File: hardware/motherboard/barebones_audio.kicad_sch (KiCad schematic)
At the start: 71 parts, among them J22 SJ2-35894B-SMT-TR, SW4 EC05E1220401, U34 ES8316, U35 TS3A227EYFFR, U37 TPA2012D2RTJT, U75 STM32L433VCT6, U76 PCA9306DCTR, Y6 ABS07-32.768KHZ-T

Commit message: pushed many changes and added dedicated bms module
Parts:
- removed R129: 330k, Resistor_SMD:R_0603_1608Metric, symbol Device:R
- removed R130: 10k, Resistor_SMD:R_0603_1608Metric, symbol Device:R
- removed R250, R251, R252: 4.7k, Resistor_SMD:R_0402_1005Metric, symbol Device:R
- removed SW4: EC05E1220401, barebones:SW-SMD_EC05E1220401, symbol EC05E1220401:EC05E1220401
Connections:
- net AGND is gone; now on net GND: U34.17 (CPGND), U34.23 (AGND), U34.33 (EP), U34.5 (DGND)
- net SCL_AUDIO is gone; now on net I2C7_SCL_M0: R132.2, U35.C3 (SCL)
- net SDA_AUDIO is gone; now on net I2C7_SDA_M0: R218.2, U35.B3 (SDA)
- net ES_LOUT: no longer U34.20 (LOUT)
- net ES_ROUT: no longer U34.19 (ROUT)
- net HP_JACK_RING_2: no longer J22.4, U35.D1 (RING2)
- net HP_JACK_SLEEVE: no longer J22.1, U35.D3 (SLEEVE)
- net VCC_1V8_S0: now also R132.1, R216.1, R217.1, R218.1
- net VCC_3V3_S3: no longer R132.1, R216.1, R217.1, R218.1
- net HP_RING_1: now reaches J22.3
- net HP_RING_1: now also U34.19 (ROUT)
- net EN_CHAN_A_0: no longer names the net of U75.23 (PA0)
- net EN_CHAN_B_0: no longer names the net of U75.24 (PA1)
- net HP_DET_TRIGGER renamed HP_DET
- net HP_INT: no longer names the net of U34.12 (GPIO3)
- net HP_JACK_TIP renamed HP_TIP
- net HP_TIP: now also U34.20 (LOUT)
- net I2S0_LRCK_TX renamed I2S0_LRCK
- net I2S0_SCLK_TX renamed I2S0_SCLK
- new net HP_RING_2: J22.4, U35.D1 (RING2)
- new net HP_SLEEVE: J22.1, U35.D3 (SLEEVE)
- no-connect marks 8 -> 11
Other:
- moved on the sheet: C396, C397, C398, C399, C400, C401, C402, C403, C404, C405, C406, C407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

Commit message: arranged the schematics in every sheet
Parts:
- removed C413, C415, C419, C424: 1uF, Capacitor_SMD:C_0603_1608Metric, symbol Device:C
- added C425, C427, C428, C429: 1uF, Capacitor_SMD:C_0603_1608Metric, symbol Device:C
- added C539: 100nF, Capacitor_SMD:C_0603_1608Metric, symbol Device:C
- added J13, J8: SM02B-GHS-TB_LF__SN_, barebones:JST_SM02B-GHS-TB_LF__SN_, symbol SM02B-GHS-TB_LF__SN_:SM02B-GHS-TB_LF__SN_
- added J19: SM06B-SRSS-TB_LF__SN_, SM06B-SRSS-TB_LF__SN_:JST_SM06B-SRSS-TB_LF__SN_, symbol SM06B-SRSS-TB_LF__SN_:SM06B-SRSS-TB_LF__SN_
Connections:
- net GND: now also C425.2, C427.2, C428.2, C429.2, C539.2, J19.6, J19.S1 (SHIELD), J19.S2 (SHIELD)
- net NRST_90: now also J19.4
- net SWCLK_49: now also J19.3
- net SWDIO_72: now also J19.2
- net SWO_89: now also J19.5
- net VCC_3V3_ALW: now also C539.1, J19.1
- net SPK_OUT_L+ renamed SPK_OUT_L_1+
- net SPK_OUT_L_1+: now also C427.1, J8.1
- net SPK_OUT_L- renamed SPK_OUT_L_1-
- net SPK_OUT_L_1-: now also C425.1, J8.2
- net SPK_OUT_R+ renamed SPK_OUT_R_1+
- net SPK_OUT_R_1+: now also C428.1, J13.1
- net SPK_OUT_R- renamed SPK_OUT_R_1-
- net SPK_OUT_R_1-: now also C429.1, J13.2
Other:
- note added: "AUDIO SUBSYSTEM"
- note added: "EMBEDDED CONTROLLER"
- note added: "LEFT SPEAKER"
- note added: "NOTE THIS CHIPS"
- note added: "RIGHT SPEAKER"
- note added: "finish this connection properly"
- note removed: "DIGITAL MEMS MIC"
- moved on the sheet: C396, C397, C398, C399, C400, C401, C402, C403, C404, C405, C406, C407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

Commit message: connected hierarchical labels with net labels in the root sheet
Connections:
- net NRST_14: now also J19.4
- net NRST_90: no longer J19.4, U75.90 (PB4(NJTRST))
- no-connect marks 11 -> 14
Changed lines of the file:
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@@
 	)
 	(no_connect
+		(at 368.3 154.94)
+	)
+	(no_connect
 		(at 368.3 83.82)
 	)
@@
 	)
 	(no_connect
+		(at 368.3 162.56)
+	)
+	(no_connect
+		(at 427.99 81.28)
+	)
+	(no_connect
 		(at 318.77 60.96)
 	)
@@
 	(wire
 		(pts
-			(xy 427.99 81.28) (xy 454.66 81.28)
-		)
-		(stroke
-			(width 0)
-			(type default)
-		)
-	)
-	(wire
-		(pts
 			(xy 342.9 177.8) (xy 344.17 177.8)
 		)
@@
 	(wire
 		(pts
-			(xy 427.99 83.82) (xy 462.28 83.82)
+			(xy 427.99 83.82) (xy 467.36 83.82)
 		)
 		(stroke
@@
 	(wire
 		(pts
-			(xy 541.02 147.32) (xy 544.83 147.32)
+			(xy 541.02 147.32) (xy 553.72 147.32)
 		)
 		(stroke
@@
 		)
 	)
-	(label "NRST_90"
+	(label "NRST_14"
 		(at 509.27 187.96 0)
 		(effects
@@
 		)
 	)
+	(label "NRST_14"
+		(at 553.72 147.32 180)
+		(effects
+			(font
+				(size 1.27 1.27)
+			)
+			(justify right bottom)
+		)
+	)
 	(label "VDD_50"
 		(at 346.71 180.34 0)
@@
 		)
 	)
+	(label "SWO_89"
+		(at 467.36 83.82 180)
+		(effects
+			(font
+				(size 1.27 1.27)
+			)
+			(justify right bottom)
+		)
+	)
 	(label "INL+"
 		(at 59.69 204.47 0)
@@
 		)
 	)
-	(label "NRST_90"
-		(at 454.66 81.28 180)
-		(effects
-			(font
-				(size 1.27 1.27)
-			)
-			(justify right bottom)
-		)
-	)
 	(label "HP_JACK_RING_2"
 		(at 41.91 113.03 0)
@@
 		)
 	)
-	(hierarchical_label "NRST_14"
-		(shape input)
-		(at 544.83 147.32 0)
-		(effects
-			(font
-				(size 1.27 1.27)
-			)
-			(justify left)
-		)
-	)
 	(hierarchical_label "I2C7_SDA_M0"
 		(shape input)
@@
 		(effects
 			(font
-				(size 1.27 1.27)
-			)
-			(justify left)
-		)
-	)
-	(hierarchical_label "SWO_89"
-		(shape input)
-		(at 462.28 83.82 0)
-		(effects
-			(font

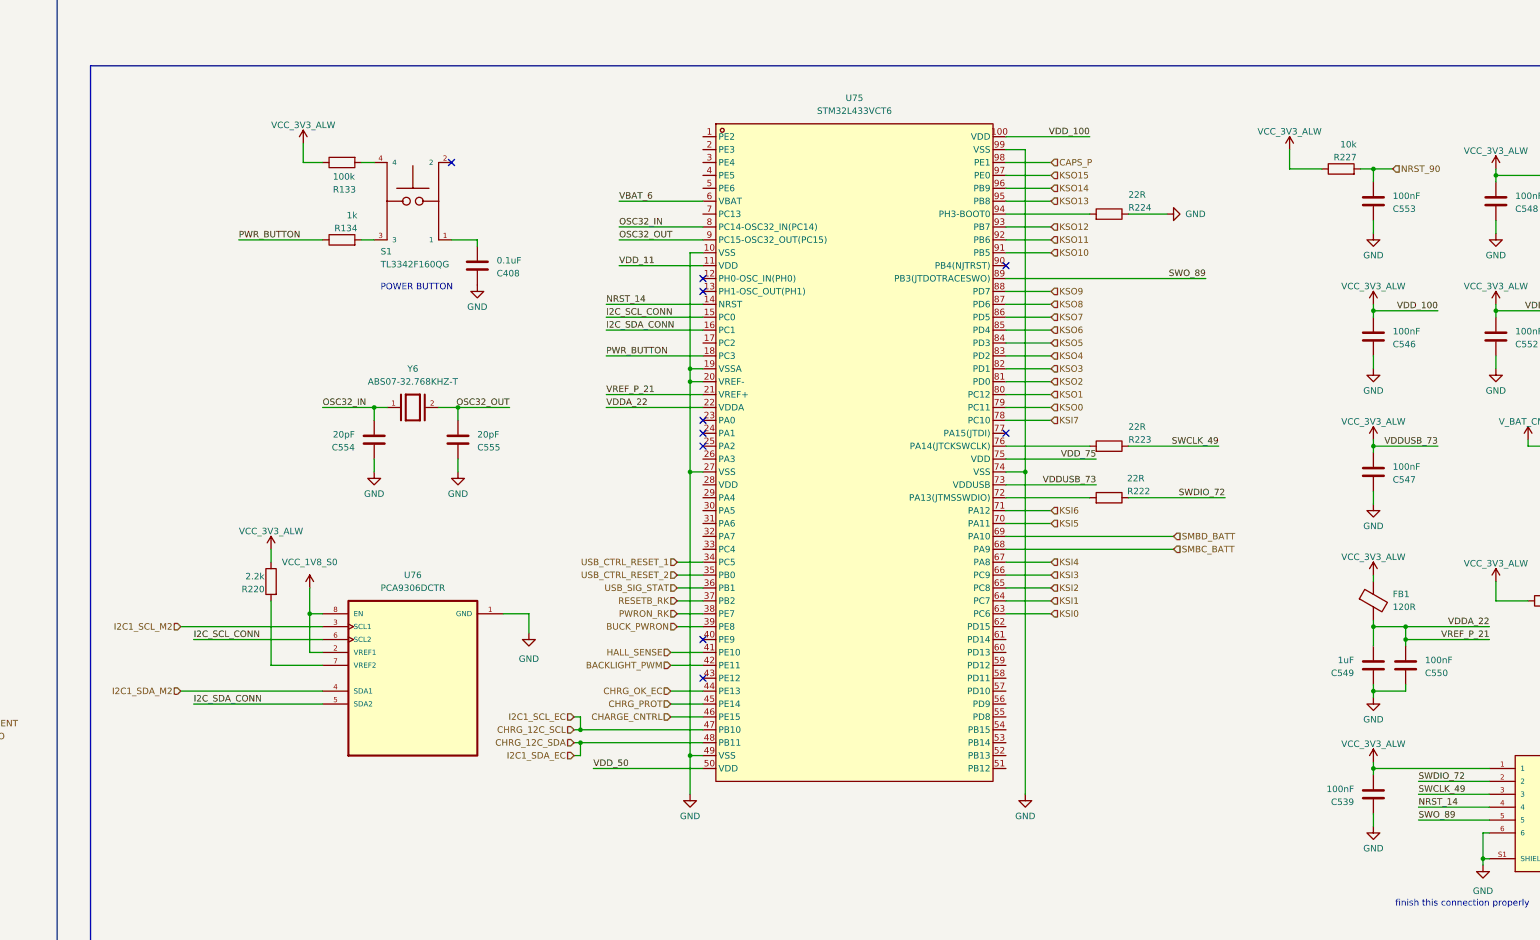
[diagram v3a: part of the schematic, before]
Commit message: removed unused components and connections
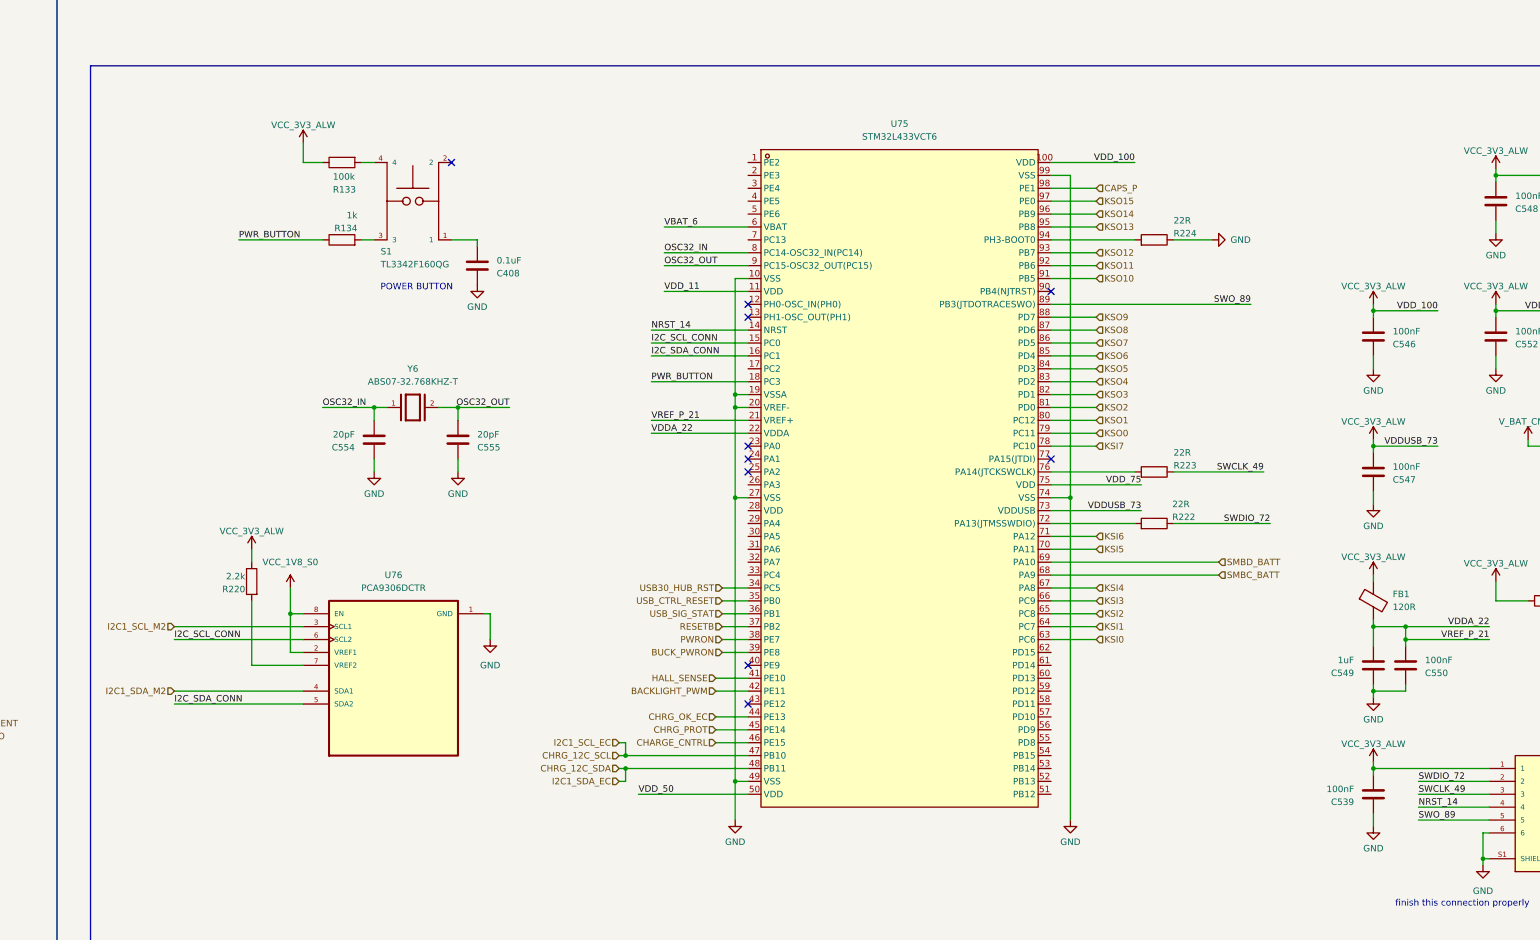
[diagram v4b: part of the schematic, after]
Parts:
- removed C553: 100nF, Capacitor_SMD:C_0603_1608Metric, symbol Device:C
- removed R227: 10k, Resistor_SMD:R_0603_1608Metric, symbol Device:R
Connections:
- net PWRON_RK renamed PWRON
- net RESETB_RK renamed RESETB
- net USB_CTRL_RESET_1 renamed USB30_HUB_RST
- net USB_CTRL_RESET_2 renamed USB_CTRL_RESET
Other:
- moved on the sheet: R220, R222, R223, R224, U75, U76

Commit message: updated last changes
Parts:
- removed C397, C406, C539, C546, C547, C552: 100nF, Capacitor_SMD:C_0603_1608Metric, symbol Device:C
- removed C398: 10uF, Capacitor_SMD:C_0603_1608Metric, symbol Device:C
- removed C414: 1uF, Capacitor_SMD:C_0603_1608Metric, symbol Device:C
- removed C554: 20pF, Capacitor_SMD:C_0603_1608Metric, symbol Device:C
- removed FB1: 120R, Inductor_SMD:L_0402_1005Metric, symbol Device:FerriteBead
- removed J13, J8: SM02B-GHS-TB_LF__SN_, barebones:JST_SM02B-GHS-TB_LF__SN_, symbol SM02B-GHS-TB_LF__SN_:SM02B-GHS-TB_LF__SN_
- removed J22: SJ2-35894B-SMT-TR, barebones:CUI_SJ2-35894B-SMT-TR, symbol SJ2-35894B-SMT-TR:SJ2-35894B-SMT-TR
- removed MK1: SPH0645LM4H-B, barebones:MIC_SPH0645LM4H-B, symbol SPH0645LM4H-B:SPH0645LM4H-B
- removed MK2: CMM-2718AT-3817NC-TR, CMM-2718AT-3817NC-TR:MIC_CMM-2718AT-3817NC-TR, symbol CMM-2718AT-3817NC-TR:CMM-2718AT-3817NC-TR
- removed NT3, NT4: NetTie_2, NetTie:NetTie-2_SMD_Pad0.5mm, symbol Device:NetTie_2
- removed R133: 100k, Resistor_SMD:R_0603_1608Metric, symbol Device:R
- removed R216, R217, R218: 4.7k, Resistor_SMD:R_0603_1608Metric, symbol Device:R
- removed R220: 2.2k, Resistor_SMD:R_0402_1005Metric, symbol Device:R
- removed U75: STM32L433VCT6, barebones:QFP50P1600X1600X160-100N, symbol STM32L433VCT6:STM32L433VCT6
- removed U76: PCA9306DCTR, barebones:SOP65P400X130-8N, symbol PCA9306DCTR:PCA9306DCTR
- added C413, C473, C475, C621, C698, C709, C711, C713, C715, C717, C718, C719, C720, C721, C722: 0.1uF, Capacitor_SMD:C_0201_0603Metric, symbol Device:C
- added C415, C545, C573: 10uF, Capacitor_SMD:C_0603_1608Metric, symbol Device:C
- added C431, C458: 0.1uF, Capacitor_SMD:C_0402_1005Metric, symbol Device:C
- added C477, C478, C574, C615, C707, C708, C710, C712, C714: 1uF, Capacitor_SMD:C_0402_1005Metric, symbol Device:C
- added C544: 4.7uF, Capacitor_SMD:C_0402_1005Metric, symbol Device:C
- added C622: 20pF, Capacitor_SMD:C_0201_0603Metric, symbol Device:C
- added FL2, FL3: BLM18PG121SZ1D, barebones:BEADC1608X95N, symbol BLM18PG121SZ1D:BLM18PG121SZ1D
- added J14, J15: S2B-PH-K-S_LF__SN_, barebones:JST_S2B-PH-K-S_LF__SN_, symbol S2B-PH-K-S_LF__SN_:S2B-PH-K-S_LF__SN_
- added J16: SM04B-SRSS-TB_LF__SN_, barebones:JST_SM04B-SRSS-TB_LF__SN_, symbol SM04B-SRSS-TB_LF__SN_:SM04B-SRSS-TB_LF__SN_
- added J4, J8: SJ3-350114B, barebones:SAMESKY_SJ3-350114B, symbol SJ3-350114B:SJ3-350114B
- added R148, R149: 2.2k, Resistor_SMD:R_0201_0603Metric, symbol Device:R
- added R156, R157, R158: 4.7k, Capacitor_SMD:C_0201_0603Metric, symbol Device:R
- added R192, R193, R243, R244: 10k, Resistor_SMD:R_0201_0603Metric, symbol Device:R
- added U13: STM32U083MCT6, barebones:TQFP-80_L12.0-W12.0-P0.50-LS14.0-BL, symbol STM32U083MCT6:STM32U083MCT6
- added U16, U17: TPS22919DCK, Package_TO_SOT_SMD:SOT-363_SC-70-6, symbol Power_Management:TPS22919DCK
- C396, C408, C555: footprint Capacitor_SMD:C_0603_1608Metric -> Capacitor_SMD:C_0201_0603Metric
- C399, C407, C550, C551, C560: value 100nF -> 0.1uF; footprint Capacitor_SMD:C_0603_1608Metric -> Capacitor_SMD:C_0201_0603Metric
- C403, C412, C418, C420, C423, C426, C428, C429, C542, C549: footprint Capacitor_SMD:C_0603_1608Metric -> Capacitor_SMD:C_0402_1005Metric
- C405, C548: value 100nF -> 10uF
- C425: value 1uF -> 0.1uF; footprint Capacitor_SMD:C_0603_1608Metric -> Capacitor_SMD:C_0201_0603Metric
- C427: value 1uF -> 0.1uF; footprint Capacitor_SMD:C_0603_1608Metric -> Capacitor_SMD:C_0402_1005Metric
- J19: footprint SM06B-SRSS-TB_LF__SN_:JST_SM06B-SRSS-TB_LF__SN_ -> barebones:JST_SM06B-SRSS-TB_LF__SN_
- R131, R134, R141, R219, R221, R222, R223: footprint Resistor_SMD:R_0603_1608Metric -> Resistor_SMD:R_0201_0603Metric
- R132: footprint Resistor_SMD:R_0603_1608Metric -> Capacitor_SMD:C_0201_0603Metric
- R224: value 22R -> 10k; footprint Resistor_SMD:R_0603_1608Metric -> Resistor_SMD:R_0201_0603Metric
- U35: footprint TS3A227EYFFR:BGA16N40P4X4_175X175X62N -> barebones:BGA16N40P4X4_175X175X62N
- Y6: footprint ABS07-32.768KHZ-T:XTAL_ABS07-32.768KHZ-T -> barebones:XTAL_ABS07-32.768KHZ-T
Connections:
- net ES_LOUT is gone; now on net HP_TIP: C418.2
- net ES_ROUT is gone; now on net HP_RING_1: C423.2
- net GNDREF is gone; now on net GND: U34.18 (CPGNDREF)
- net HP_JACK_RING_2 is gone; now on net HP_RING_2: U35.C4 (RING2_SENSE)
- net HP_JACK_SLEEVE is gone; now on net HP_SLEEVE: U35.D4 (SLEEVE_SENSE)
- net VCC_1V8_S0 is gone; now on net AUDIO_PWR_1V8: R132.1, U34.3 (DVDD), U34.4 (PVDD)
- net VCC_ES_CE is gone; now on net AUDIO_PWR_1V8: R219.2
- net BACKLIGHT_PWM: now also U13.30 (PB1)
- net BUCK_PWRON: now also U13.28 (PC5)
- net CAPS_P: now also U13.80 (PB9)
- net CHRG_12C_SCL: now also R244.2, U13.35 (PB10)
- net CHRG_12C_SDA: now also R243.2, U13.36 (PB11)
- net CHRG_OK_EC: now also U13.31 (PB2)
- net CHRG_PROT: now also U13.32 (PE7)
- net DACVREF: now also C415.2; no longer C401.2
- net GND: now also C401.2, C405.2, C425.1, C413.2, C415.1, C431.2, C458.2, C473.2, C475.2, C477.2, C478.2, C544.2, C545.2, C573.2, C621.2, C622.2, C698.2, C707.2, C708.2, C709.2, C710.2, C711.2, C712.2, C713.2, C714.2, C715.2, C717.2, C718.2, C719.2, C720.2, C721.2, C722.2, J16.1, J16.S1 (SHIELD), J16.S2 (SHIELD), J8.1, J8.4_1, J8.4_2, R192.1, R193.1, U13.1 (VSS), U13.14 (VSSA/VREF-), U13.21 (VSS), U13.37 (VSS), U13.59 (VSS), U16.2 (GND), U17.2 (GND); no longer C401.1, C405.1, C425.2, J19.6
- net HALL_SENSE: now also U13.29 (PB0)
- net HP_DET: now also J4.5
- net HP_RING_1: now also J4.3
- net HP_RING_2: now also J4.4_1, J4.4_2
- net HP_SLEEVE: now also J4.1
- net HP_TIP: now also J4.2
- net I2C7_SDA_M0: now also R156.2
- net INT_AUDIO: now also R157.2
- net KSI0: now also U13.46 (PD11)
- net KSI1: now also U13.47 (PD12)
- net KSI2: now also U13.48 (PD13)
- net KSI3: now also U13.49 (PC6)
- net KSI4: now also U13.50 (PC7)
- net KSI5: now also U13.51 (PC8)
- net KSI6: now also U13.52 (PC9)
- net KSI7: now also U13.62 (PA15)
- net KSO0: now also U13.63 (PC10)
- net KSO1: now also U13.64 (PC11)
- net KSO10: now also U13.73 (PB3)
- net KSO11: now also U13.74 (PB4)
- net KSO12: now also U13.75 (PB5)
- net KSO13: now also U13.76 (PB6)
- net KSO14: now also U13.77 (PB7)
- net KSO15: now also U13.79 (PB8)
- net KSO2: now also U13.65 (PC12)
- net KSO3: now also U13.66 (PD0)
- net KSO4: now also U13.67 (PD1)
- net KSO5: now also U13.68 (PD2)
- net KSO6: now also U13.69 (PD3)
- net KSO7: now also U13.70 (PD4)
- net KSO8: now also U13.71 (PD5)
- net KSO9: now also U13.72 (PD6)
- net LIN2: now also C574.1; no longer C405.2
- net MICBIAS: now also R148.1, R149.2
- net MIC_PRESENT: now also R158.2
- net OSC32_IN: now also C622.1, U13.5 (PC14-OSC32_IN)
- net OSC32_OUT: now also U13.6 (PC15-OSC32_OUT)
- net PVDD: now also C431.1, C458.1, C545.1, C573.1, FL2.1
- net PWRON: now also U13.27 (PC4)
- net PWR_BUTTON: now also U13.56 (PA11[PA9])
- net RESETB: now also U13.26 (PA7)
- net RIN2: now also C615.1
- net SMBC_BATT: now also U13.54 (PA9)
- net SMBD_BATT: now also U13.55 (PA10)
- net SPK_OUT_L_1+: now also C477.1, J14.1; no longer C427.1
- net SPK_OUT_L_1-: now also C478.1, J14.2; no longer C425.1
- net SPK_OUT_R_1+: now also J15.1
- net SPK_OUT_R_1-: now also J15.2
- net USB30_HUB_RST: now also U13.23 (PA4)
- net USB_CTRL_RESET: now also U13.24 (PA5)
- net USB_SIG_STAT: now also U13.25 (PA6)
- net VCC_3V3_ALW: now also C621.1, C707.1, C708.1, C709.1, C710.1, C711.1, C712.1, C713.1, C714.1, C715.1, FL3.1, R243.1, R244.1, U13.2 (VDD), U13.22 (VDD), U13.38 (VDD), U13.60 (VDDUSB); no longer C548.1
- net V_BAT_CMOS: now also U13.3 (VBAT)
- net at R223.2: now also U13.61 (PA14)
- net at R222.2: now also U13.58 (PA13)
- net at R224.2: now also U13.78 (PF3-BOOT0)
- net RIN1: now reaches U34.29 (RIN1)
- net RIN1: now also C425.2
- net AVDD renamed AUDIO_PWR_IN
- net AUDIO_PWR_IN: now also C473.1, C544.1, C719.1, U16.5 (QOD), U16.6 (OUT)
- net CPVDD renamed AUDIO_PWR_1V8
- net AUDIO_PWR_1V8: now also C401.1, C405.1, C413.1, C475.1, C722.1, R156.1, R157.1, R158.1, U17.5 (QOD), U17.6 (OUT)
- net NRST_14 renamed NRST
- net NRST: now also U13.9 (PF2-NRST)
- net SWCLK_49 renamed SWCLK
- net SWDIO_72 renamed SWDIO
- net SWO_89 renamed LPUART_TX
- net LPUART_TX: now also U13.19 (PA2)
- net VCC_3V3_S3 renamed VCC_3V3_S0
- net VCC_3V3_S0: now also FL2.2
- net VDDA_22 renamed VDDA
- net VDDA: now also C698.1, FL3.2, U13.15 (VREF+), U13.16 (VDDA)
- new net AUDIO_PWR_1: C720.1, C721.1, R193.2, U17.1 (IN), U17.3 (ON)
- new net AUDIO_PWR_2: C717.1, C718.1, R192.2, U16.1 (IN), U16.3 (ON)
- new net BATT_PRES: U13.34 (PE9)
- new net BK_0_PG: U13.44 (PD9)
- new net BK_1_PG: U13.43 (PD8)
- new net CHRG_CTRL: U13.33 (PE8)
- new net FAN_PWM: J16.2, U13.53 (PA8)
- new net FAN_TACH: J16.4, U13.17 (PA0)
- new net HLL_SENSOR: U13.40 (PB13)
- new net INT_ALS: U13.18 (PA1)
- new net LPUART_RX: J19.6, U13.20 (PA3)
- new net LP_INDICATOR: U13.39 (PB12)
- new net MIC_RING_1: C615.2, J8.3, R148.2
- new net MIC_TIP: C574.2, J8.2, R149.1
- new net VCC_5V0_SYS: C427.1, C548.1, J16.3
- no-connect marks 14 -> 17
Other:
- note removed: "NOTE THIS CHIPS"
- moved on the sheet: C396, C399, C400, C402, C403, C407, C408, C412, C418, C523, C525, C542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

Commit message: started routing on LPDDR4x RAM
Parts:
- removed J14: S2B-PH-K-S_LF__SN_, barebones:JST_S2B-PH-K-S_LF__SN_, symbol S2B-PH-K-S_LF__SN_:S2B-PH-K-S_LF__SN_
- added J5: SM04B-SRSS-TB_LF__SN_, barebones:JST_SM04B-SRSS-TB_LF__SN_, symbol SM04B-SRSS-TB_LF__SN_:SM04B-SRSS-TB_LF__SN_
- added R254: 10k, Resistor_SMD:R_0201_0603Metric, symbol Device:R
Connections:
- net GND: now also J5.S1 (SHIELD), J5.S2 (SHIELD)
- net SPK_OUT_L_1+: now also J5.1
- net SPK_OUT_L_1-: now also J5.2
- net SPK_OUT_R_1+: now also J5.3; no longer J15.1
- net SPK_OUT_R_1-: now also J5.4; no longer J15.2
- net VCC_3V3_ALW: now also R254.1
- net 12C1_EXTI_EC: now reaches U13.45 (PD10)
- net 12C1_EXTI_EC: now also R254.2
- net INT_ALS: no longer names the net of U13.18 (PA1)
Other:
- note added: "SPEAKER"
- note removed: "LEFT SPEAKER"
- note removed: "RIGHT SPEAKER"
